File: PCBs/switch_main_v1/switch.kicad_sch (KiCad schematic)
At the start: 1 part, among them U201 SJA1105QELY

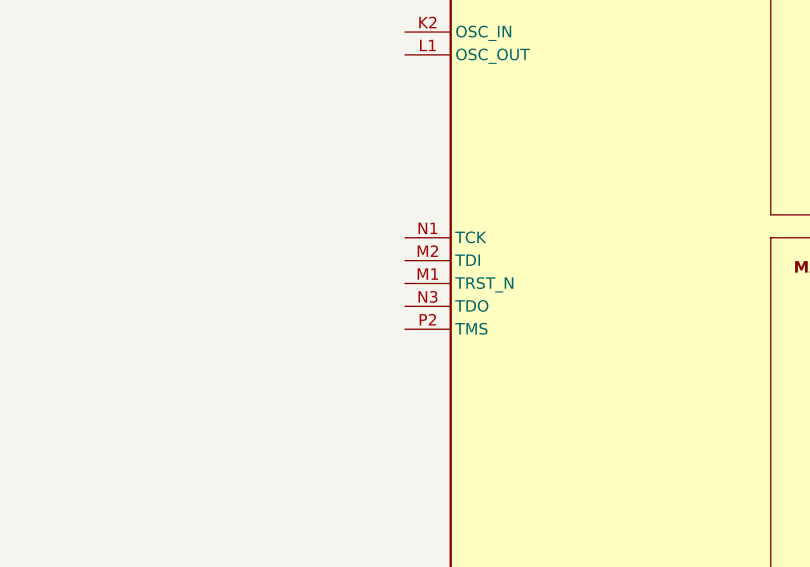
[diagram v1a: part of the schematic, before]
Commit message: Added schematic annotations
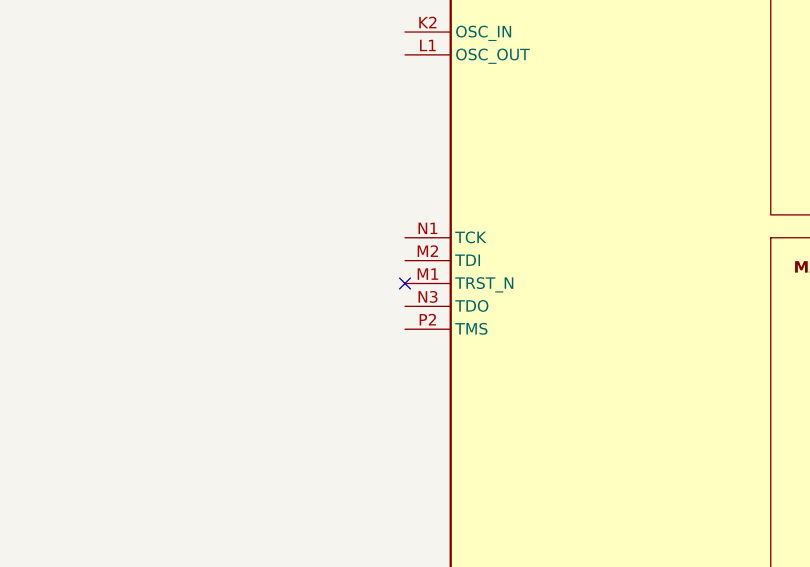
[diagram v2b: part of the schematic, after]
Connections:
- no-connect marks 0 -> 1
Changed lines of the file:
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@@
 		(color 0 0 0 0)
+	)
+	(no_connect
+		(at 116.84 187.96)
 	)
 	(wire

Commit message: Schematic progress
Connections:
- net GND: now also U201.B10 (MII2_RX_ER), U201.B3 (MII1_RX_ER), U201.F13 (MII3_RX_ER), U201.H2 (MII0_RX_ER), U201.N11 (MII4_RXD2), U201.P10 (MII4_RX_CLK/RXC), U201.P12 (MII4_RXD3), U201.P13 (MII4_RX_ER)
- net RGMII_2.RX_CTRL: now reaches U201.A11 (MII2_RX_DV/CRS_DV/RX_CTL)
- net RGMII_2.RX_D2: now reaches U201.A12 (MII2_RXD2)
- net RGMII_2.RX_D0: now reaches U201.A13 (MII2_RXD0)
- net RGMII_0.TX_D0: now reaches U201.A2 (MII0_TXD0)
- net RGMII_1.RX_CTRL: now reaches U201.A4 (MII1_RX_DV/CRS_DV/RX_CTL)
- net RGMII_1.RX_D2: now reaches U201.A5 (MII1_RXD2)
- net RGMII_1.RX_D0: now reaches U201.A6 (MII1_RXD0)
- net RGMII_1.TX_CLK: now reaches U201.A7 (MII1_TX_CLK/REF_CLK/TXC)
- net RGMII_1.TX_D3: now reaches U201.A8 (MII1_TXD3)
- net RGMII_1.TX_D1: now reaches U201.A9 (MII1_TXD1)
- net RGMII_0.TX_D1: now reaches U201.B1 (MII0_TXD1)
- net RGMII_2.RX_D3: now reaches U201.B11 (MII2_RXD3)
- net RGMII_2.RX_D1: now reaches U201.B12 (MII2_RXD1)
- net RGMII_2.RX_CLK: now reaches U201.B14 (MII2_RX_CLK/RXC)
- net RGMII_1.RX_D3: now reaches U201.B4 (MII1_RXD3)
- net RGMII_1.RX_D1: now reaches U201.B5 (MII1_RXD1)
- net RGMII_1.RX_CLK: now reaches U201.B6 (MII1_RX_CLK/RXC)
- net RGMII_1.TX_CTRL: now reaches U201.B7 (MII1_TTX_EN/TX_CTL)
- net RGMII_1.TX_D2: now reaches U201.B8 (MII1_TXD2)
- net RGMII_1.TX_D0: now reaches U201.B9 (MII1_TXD0)
- net RGMII_0.TX_D3: now reaches U201.C1 (MII0_TXD3)
- net RGMII_2.TX_CTRL: now reaches U201.C13 (MII2_TX_EN/TX_CTL)
- net RGMII_2.TX_CLK: now reaches U201.C14 (MII2_TX_CLK/REF_CLK/TXC)
- net RGMII_0.TX_D2: now reaches U201.C2 (MII0_TXD2)
- net RGMII_0.TX_CLK: now reaches U201.D1 (MII0_TX_CLK/REF_CLK/TXC)
- net RGMII_2.TX_D2: now reaches U201.D13 (MII2_TXD2)
- net RGMII_2.TX_D3: now reaches U201.D14 (MII2_TXD3)
- net RGMII_0.TX_CTRL: now reaches U201.D2 (MII0_TX_EN/TX_CTL)
- net RGMII_0.RX_D0: now reaches U201.E1 (MII0_RXD0)
- net RGMII_2.TX_D0: now reaches U201.E13 (MII2_TXD0)
- net RGMII_2.TX_D1: now reaches U201.E14 (MII2_TXD1)
- net RGMII_0.RX_CLK: now reaches U201.E2 (MII0_RX_CLK/RXC)
- net RGMII_0.RX_D2: now reaches U201.F1 (MII0_RXD2)
- net RGMII_0.RX_D1: now reaches U201.F2 (MII0_RXD1)
- net RGMII_0.RX_CTRL: now reaches U201.G1 (MII0_RX_DV/CRS_DV/RX_CTL)
- net RGMII_3.RX_D3: now reaches U201.G13 (MII3_RXD3)
- net RGMII_3.RX_CTRL: now reaches U201.G14 (MII3_RX_DV/CRS_DV/RX_CTL)
- net RGMII_0.RX_D3: now reaches U201.G2 (MII0_RXD3)
- net CLK_OUT: now reaches U201.H1 (CLK_OUT)
- net RGMII_3.RX_D1: now reaches U201.H13 (MII3_RXD1)
- net RGMII_3.RX_D2: now reaches U201.H14 (MII3_RXD2)
- net RGMII_3.RX_CLK: now reaches U201.J13 (MII3_RX_CLK/RXC)
- net RGMII_3.RX_D0: now reaches U201.J14 (MII3_RXD0)
- net RGMII_3.TX_CTRL: now reaches U201.K13 (MII3_TX_EN/TX_CTL)
- net RGMII_3.TX_CLK: now reaches U201.K14 (MII3_TX_CLK/REF_CLK/TXC)
- net RGMII_3.TX_D2: now reaches U201.L13 (MII3_TXD2)
- net RGMII_3.TX_D3: now reaches U201.L14 (MII3_TXD3)
- net RGMII_3.TX_D0: now reaches U201.M13 (MII3_TXD0)
- net RGMII_3.TX_D1: now reaches U201.M14 (MII3_TXD1)
- net RMII.RX_D0: now reaches U201.N10 (MII4_RXD0)
- net RMII.CRS_DV: now reaches U201.N12 (MII4_RX_DV/CRS_DV/RX_CTL)
- net PTP_CLK: now reaches U201.N4 (PTP_CLK)
- net SPI.MOSI: now reaches U201.N5 (SDI)
- net SPI.CS: now reaches U201.N6 (SS_N)
- net RMII.TX_D1: now reaches U201.N7 (MII4_TXD1)
- net RMII.REF_CLK: now reaches U201.N9 (MII4_TX_CLK/REF_CLK/TXC)
- net RMII.RX_D1: now reaches U201.P11 (MII4_RXD1)
- net RST: now reaches U201.P3 (RST_N)
- net SPI.MISO: now reaches U201.P4 (SDO)
- net SPI.SCK: now reaches U201.P5 (SCK)
- net RMII.TX_D0: now reaches U201.P7 (MII4_TXD0)
- net RMII.TX_EN: now reaches U201.P9 (MII4_TX_EN/TX_CTL)
- no-connect marks 1 -> 8

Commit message: Block diagram layout change
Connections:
- net +2V5: now reaches U201.D10 (VDDIO_MII2_1)
- net +2V5: now also U201.D11 (VDDIO_MII2_2), U201.D4 (VDDIO_MII0_1), U201.D5 (VDDIO_MII1_1), U201.D7 (VDDIO_MII1_2), U201.D8 (VDDIO_MII1_3), U201.E11 (VDDIO_MII2_3), U201.E4 (VDDIO_MII0_2), U201.G11 (VDDIO_MII3_1), U201.G4 (VDDIO_MII0_3), U201.H11 (VDDIO_MII3_2), U201.H4 (VDDIO_CLO), U201.K11 (VDDIO_MII3_3), U201.L10 (VDDIO_MII4_2), U201.L11 (VDDIO_MII4_3), U201.L5 (VDDIO_HOST), U201.L8 (VDDIO_MII4_1)
- net +1V2: now reaches U201.D6 (VDD_CORE_1)
- net +1V2: now also U201.D9 (VDD_CORE_2), U201.F11 (VDD_CORE_4), U201.F4 (VDD_CORE_3), U201.J11 (VDD_CORE_6), U201.J4 (VDD_CORE_5), U201.L6 (VDD_CORE_7), U201.L9 (VDD_CORE_8)

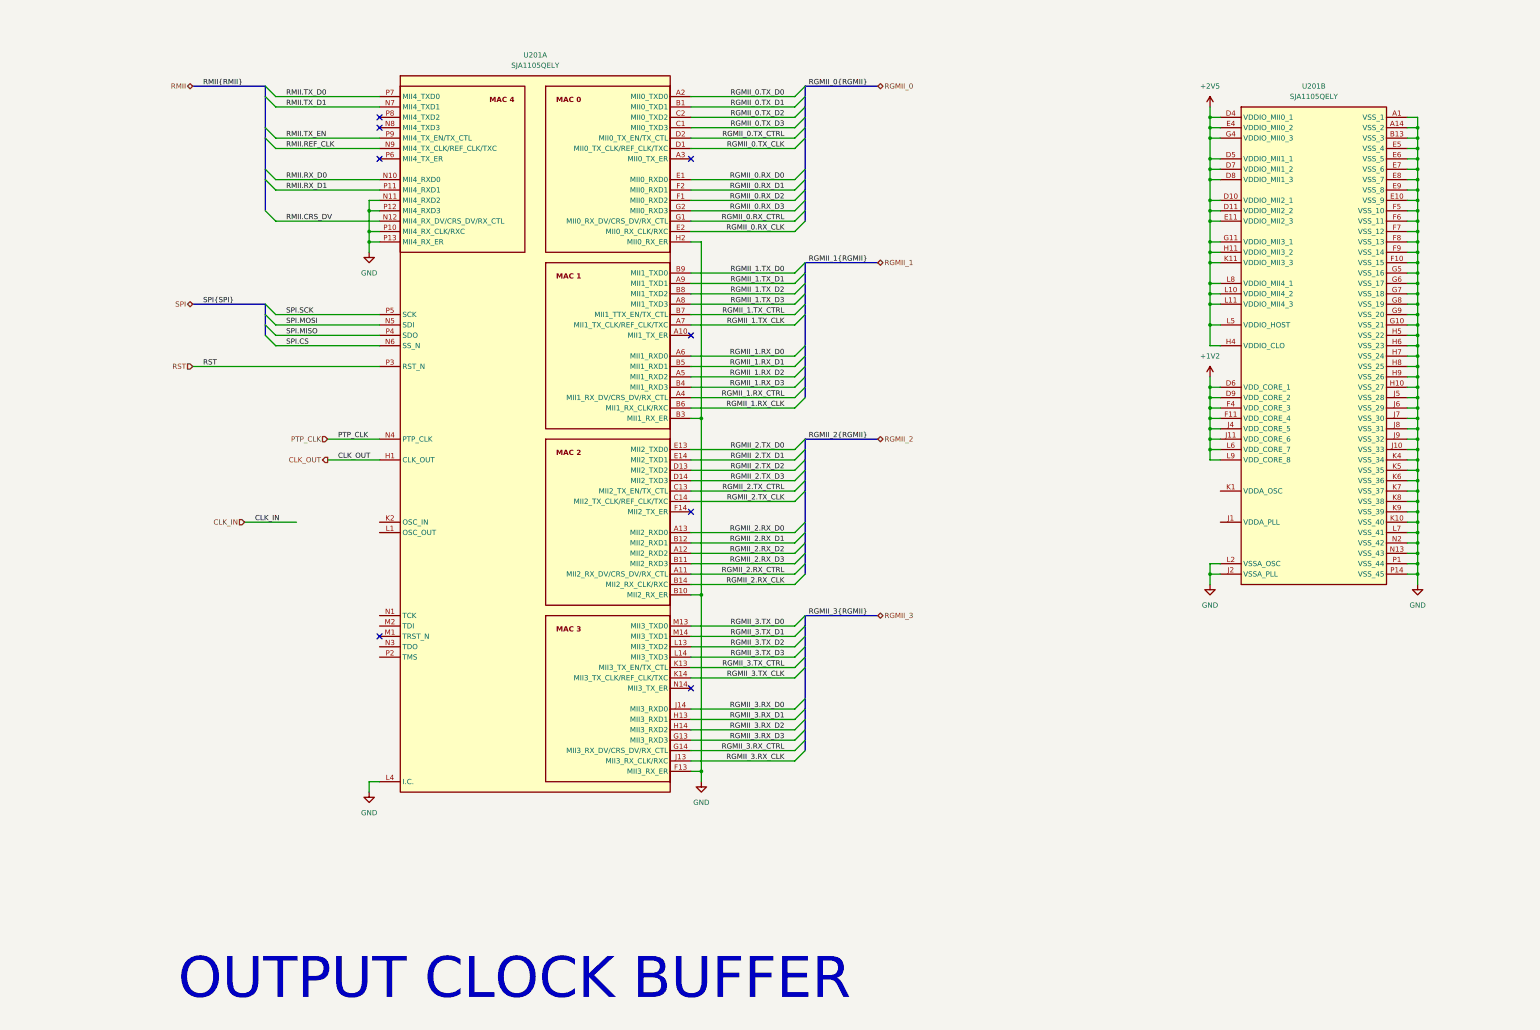
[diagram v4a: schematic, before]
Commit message: GbE part of schematic done
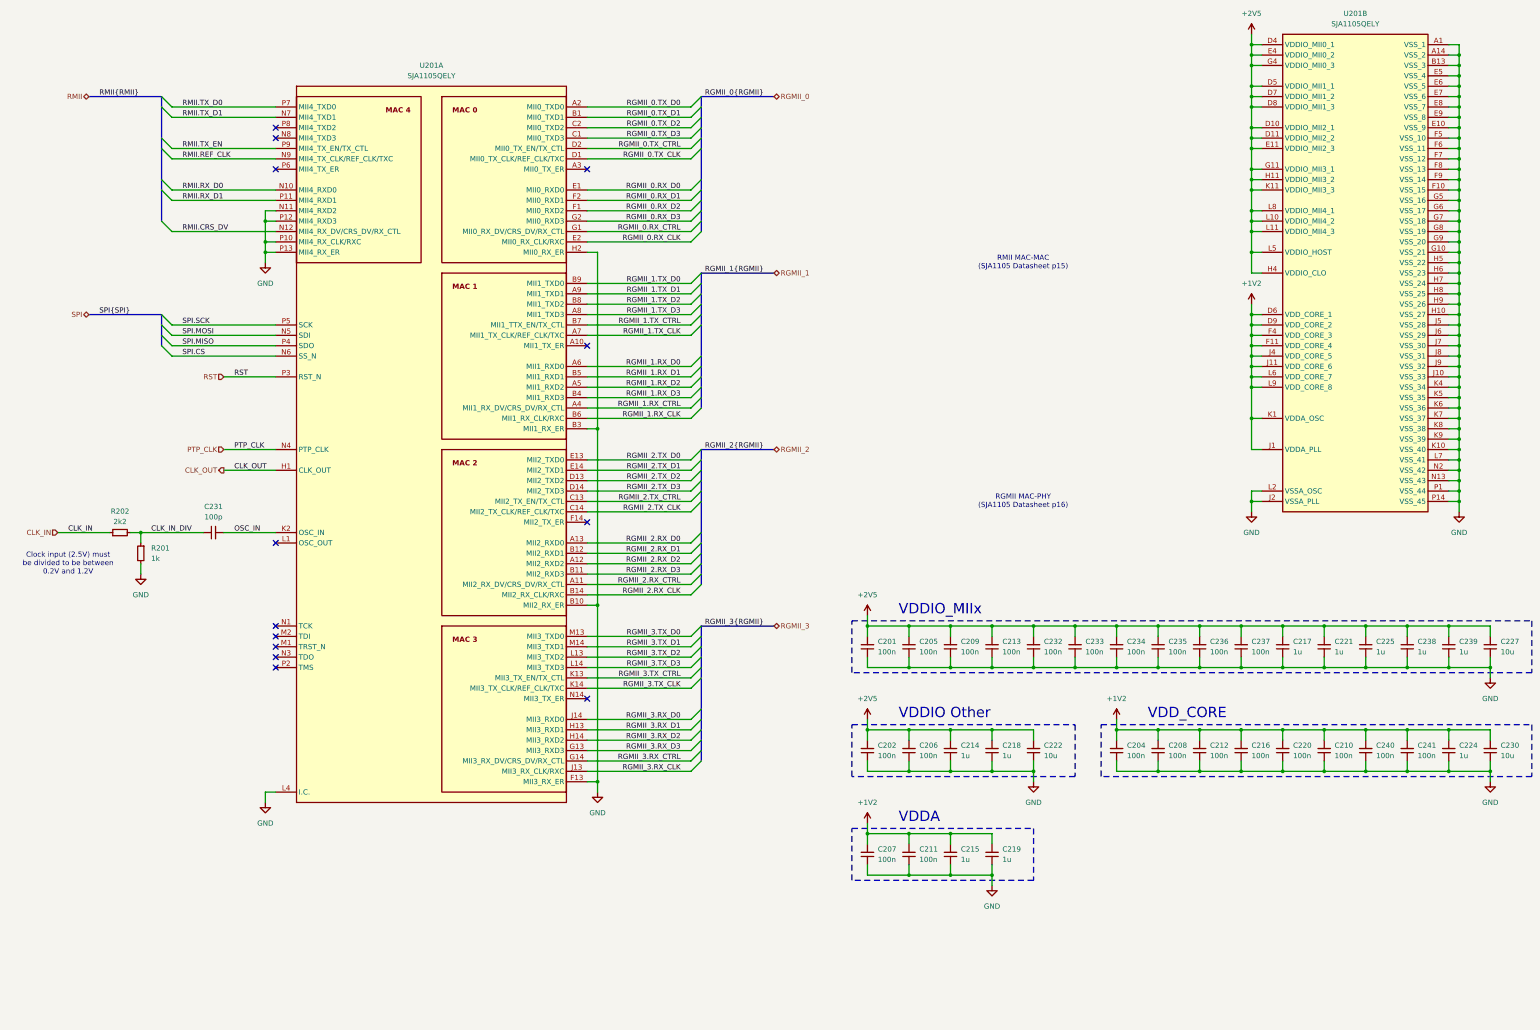
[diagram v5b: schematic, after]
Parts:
- added C201, C202, C204, C205, C206, C207, C208, C209, C210, C211, C212, C213, C216, C220, C232, C233, C234, C235, C236, C237, C240, C241: 100n, Capacitor_SMD:C_0402_1005Metric, symbol Device:C_Small
- added C214, C215, C217, C218, C219, C221, C224, C225, C238, C239: 1u, Capacitor_SMD:C_0402_1005Metric, symbol Device:C_Small
- added C222, C227, C230: 10u, Capacitor_SMD:C_0402_1005Metric, symbol Device:C_Small
- added C231: 100p, Capacitor_SMD:C_0402_1005Metric, symbol Device:C_Small
- added R201: 1k, Resistor_SMD:R_0402_1005Metric, symbol Device:R_Small
- added R202: 2k2, Resistor_SMD:R_0402_1005Metric, symbol Device:R_Small
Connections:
- net +1V2: now also U201.J1 (VDDA_PLL), U201.K1 (VDDA_OSC), C204.2, C207.2, C208.2, C210.2, C211.2, C212.2, C215.2, C216.2, C219.2, C220.2, C224.2, C230.2, C240.2, C241.2
- net +2V5: now also C201.2, C202.2, C205.2, C206.2, C209.2, C213.2, C214.2, C217.2, C218.2, C221.2, C222.2, C225.2, C227.2, C232.2, C233.2, C234.2, C235.2, C236.2, C237.2, C238.2, C239.2
- net CLK_IN: now also R202.1
- net GND: now also C201.1, C202.1, C204.1, C205.1, C206.1, C207.1, C208.1, C209.1, C210.1, C211.1, C212.1, C213.1, C214.1, C215.1, C216.1, C217.1, C218.1, C219.1, C220.1, C221.1, C222.1, C224.1, C225.1, C227.1, C230.1, C232.1, C233.1, C234.1, C235.1, C236.1, C237.1, C238.1, C239.1, C240.1, C241.1, R201.2
- net OSC_IN: now reaches U201.K2 (OSC_IN)
- net OSC_IN: now also C231.2
- new net CLK_IN_DIV: C231.1, R201.1, R202.2
- no-connect marks 8 -> 13
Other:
- note added: "Clock input (2.5V) must be divided to be between 0.2V and 1.2V"
- note added: "RGMII MAC-PHY (SJA1105 Datasheet p16)"
- note added: "RMII MAC-MAC (SJA1105 Datasheet p15)"
- note added: "VDDA"
- note added: "VDDIO Other"
- note added: "VDDIO_MIIx"
- note added: "VDD_CORE"
- note removed: "OUTPUT CLOCK BUFFER"
- company: (none) -> Ben Smith
- moved on the sheet: U201A, U201B
